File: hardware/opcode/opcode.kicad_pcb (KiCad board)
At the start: 4 copper layers, 60 parts, among them U1 74HC595, U10 74LVC1G32, U11 74LVC1G32, U12 SST39SF040, U13 SST39SF040, U14 SST39SF040, U15 SST39SF040, U16 74HC251, U17 74HC597, U18 74HC597, U19 74HC597, U2 74HC595, U20 74HC597, U21 74HC597, U22 74HC597, U23 74HC597, U24 74HC597, U25 74HC597, U26 74HC597, U27 74HC597, U28 74HC597, U29 74HC597, U3 74HC595, U30 74HC597, U4 74HC595, U5 74LVC1G00, U6 74LVC1G08, U7 74HC595, U8 74HC74, U9 74LVC1G00

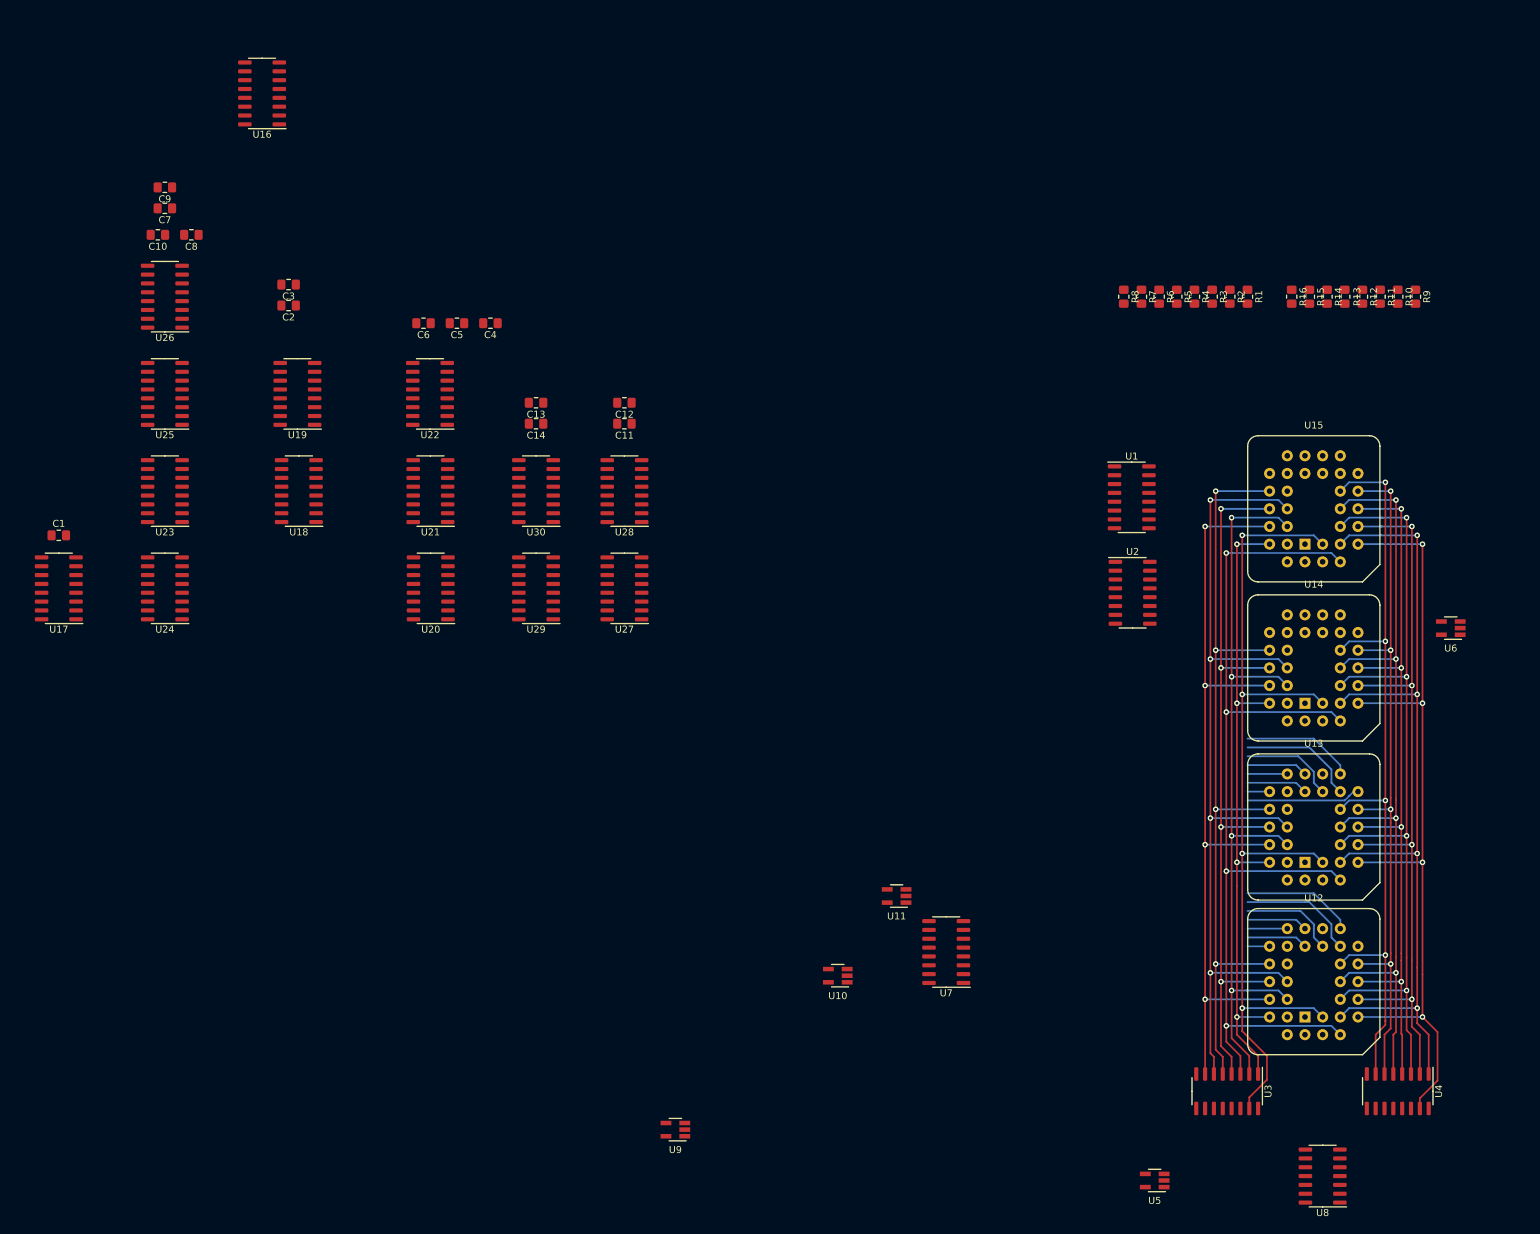
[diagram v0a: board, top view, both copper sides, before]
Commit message: Update all to Kicad 6
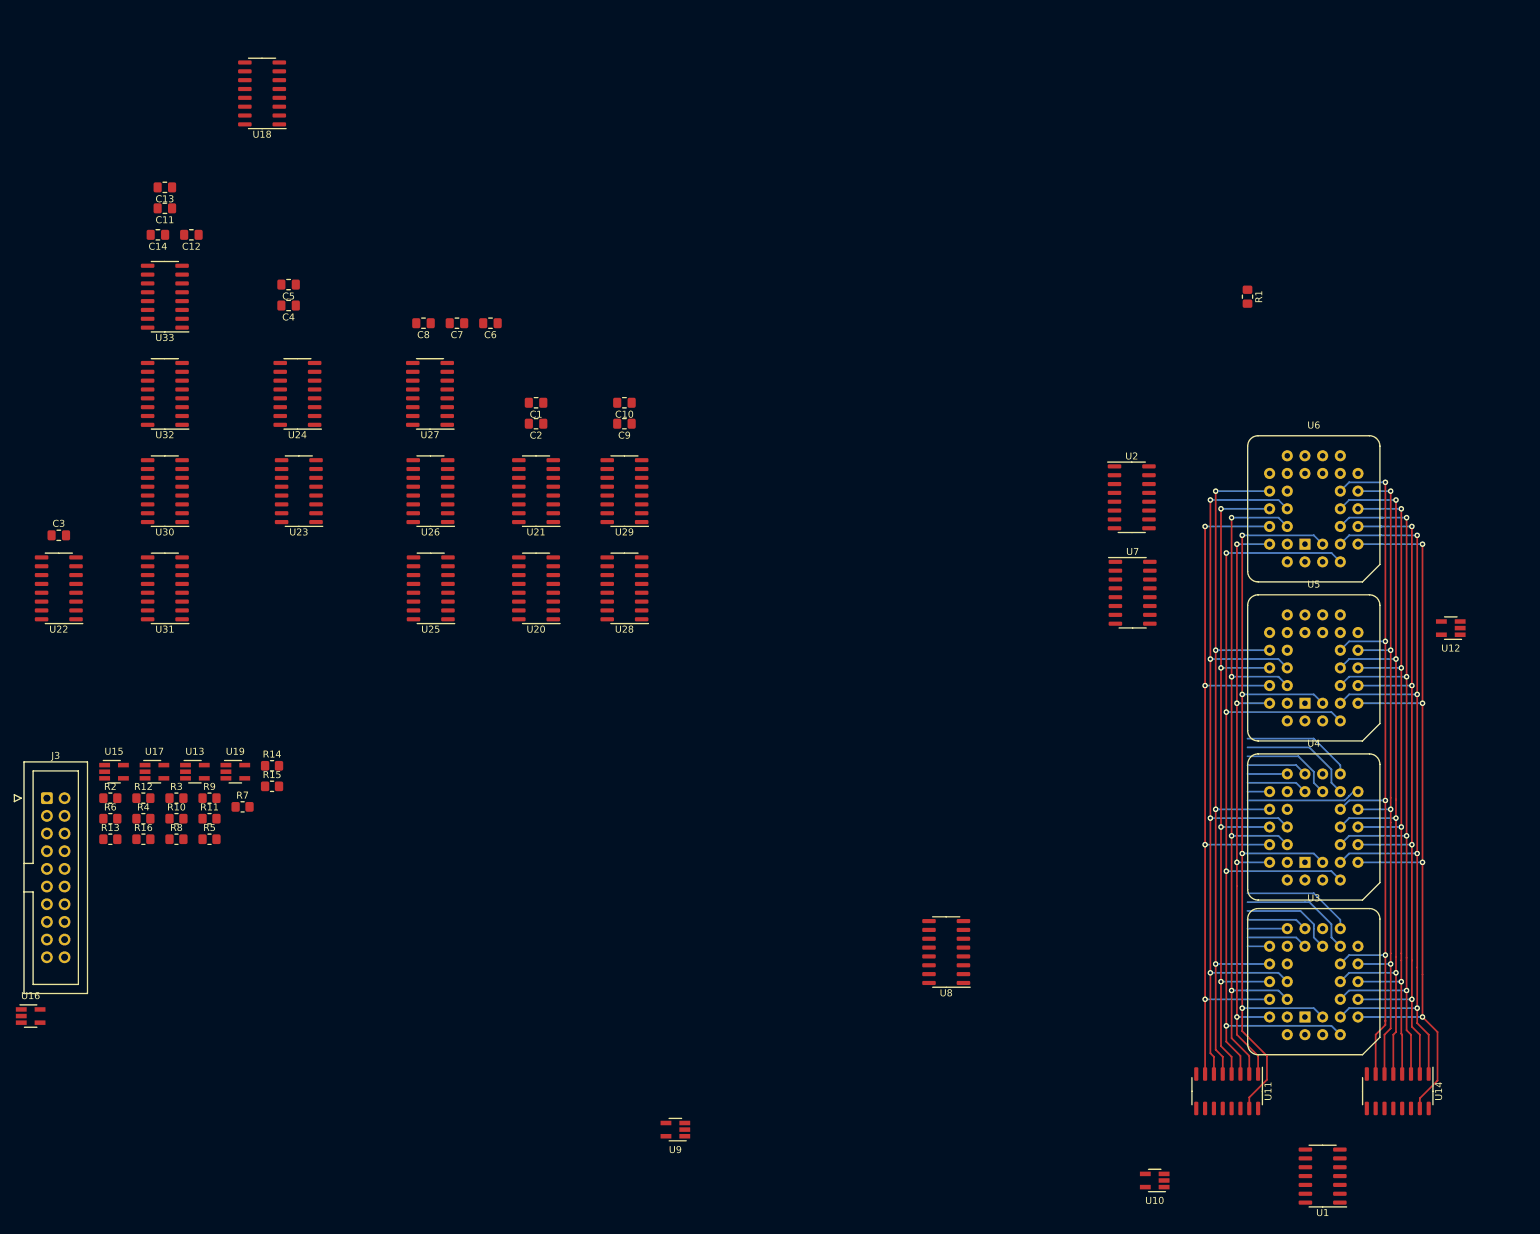
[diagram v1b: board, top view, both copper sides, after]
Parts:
- removed the U10 at (141.2, 125.5)
- removed the U11 at (149.6, 114.1)
- added J3: Conn_01x20, Connector_IDC:IDC-Header_2x10_P2.54mm_Vertical, F.Cu at (27.5, 100.0)
- added U13: 74LVC1G32, Package_TO_SOT_SMD:SOT-23-5_HandSoldering, F.Cu at (48.8, 96.2)
- added U15: 74LVC1G32, Package_TO_SOT_SMD:SOT-23-5_HandSoldering, F.Cu at (37.1, 96.2)
- added U16: 74LVC1G32, Package_TO_SOT_SMD:SOT-23-5_HandSoldering, F.Cu at (25.2, 131.3)
- added U17: 74LVC1G08, Package_TO_SOT_SMD:SOT-23-5_HandSoldering, F.Cu at (43.0, 96.2)
- added U19: 74LVC1G32, Package_TO_SOT_SMD:SOT-23-5_HandSoldering, F.Cu at (54.6, 96.2)
- moved R13 193.8 mm to (36.6, 105.9), turned to 0 degrees
- moved R10 190.9 mm to (46.1, 103.0), turned to 0 degrees
- moved R12 189.4 mm to (41.4, 100.0), turned to 0 degrees
- moved R9 187.7 mm to (50.9, 100.0), turned to 0 degrees
- moved R11 184.2 mm to (50.9, 103.0), turned to 0 degrees
- moved R16 182.5 mm to (41.4, 105.9), turned to 0 degrees
- moved R2 176.3 mm to (36.6, 100.0), turned to 0 degrees
- moved R4 168.6 mm to (41.4, 103.0), turned to 0 degrees
- moved R6 168.3 mm to (36.6, 103.0), turned to 0 degrees
- moved R14 165.9 mm to (59.9, 95.3), turned to 0 degrees
- moved R3 165.4 mm to (46.1, 100.0), turned to 0 degrees
- moved R15 164.8 mm to (59.9, 98.3), turned to 0 degrees
- moved R5 159.4 mm to (50.9, 105.9), turned to 0 degrees
- moved R8 156.9 mm to (46.1, 105.9), turned to 0 degrees
- moved R7 148.5 mm to (55.6, 101.2), turned to 0 degrees
- renumbered C13 to C1, C12 to C10, C7 to C11, C8 to C12, C9 to C13, C10 to C14, C14 to C2, C1 to C3, C2 to C4, C3 to C5, C4 to C6, C5 to C7, C6 to C8, C11 to C9, U8 to U1, U5 to U10, U3 to U11, U6 to U12, U4 to U14, U16 to U18, U1 to U2, U29 to U20, U30 to U21, U17 to U22, U18 to U23, U19 to U24, U20 to U25, U21 to U26, U22 to U27, U27 to U28, U28 to U29, U12 to U3, U23 to U30, U24 to U31, U25 to U32, U26 to U33, U13 to U4, U14 to U5, U15 to U6, U2 to U7, U7 to U8
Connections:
- U1 pad 14: Net-(U8-Pad14) -> unconnected-(U1-Pad14)
- U1 pad 6: Net-(U8-Pad6) -> unconnected-(U1-Pad6)
- U1 pad 7: Net-(U8-Pad7) -> unconnected-(U1-Pad7)
- U1 pad 9: Net-(U8-Pad9) -> unconnected-(U1-Pad9)
- U10 pad 3: Net-(U5-Pad3) -> unconnected-(U10-Pad3)
- U10 pad 5: Net-(U5-Pad5) -> unconnected-(U10-Pad5)
- U12 pad 3: Net-(U6-Pad3) -> unconnected-(U12-Pad3)
- U12 pad 5: Net-(U6-Pad5) -> unconnected-(U12-Pad5)
- U14 pad 9: Net-(U4-Pad9) -> unconnected-(U14-Pad9)
- U18 pad 6: Net-(U16-Pad6) -> unconnected-(U18-Pad6)
- U2 pad 13: /COMPR -> /COMPR_~{OE}
- U7 pad 13: /COMPR -> /COMPR_~{OE}
- U8 pad 1: Net-(U7-Pad1) -> unconnected-(U8-Pad1)
- U8 pad 15: Net-(U7-Pad15) -> unconnected-(U8-Pad15)
- U8 pad 2: Net-(U7-Pad2) -> unconnected-(U8-Pad2)
- U8 pad 3: Net-(U7-Pad3) -> unconnected-(U8-Pad3)
- U8 pad 4: Net-(U7-Pad4) -> unconnected-(U8-Pad4)
- U8 pad 5: Net-(U7-Pad5) -> unconnected-(U8-Pad5)
- U8 pad 9: Net-(U7-Pad9) -> unconnected-(U8-Pad9)
- U9 pad 3: Net-(U9-Pad3) -> unconnected-(U9-Pad3)
- U9 pad 5: Net-(U9-Pad5) -> unconnected-(U9-Pad5)

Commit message: Updated schematics and pcbs
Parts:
- added R17: 10k, riscv-serial:Jumper_3_R_0805, F.Cu at (183.5, 114.3)
- added R18: 10k, riscv-serial:Jumper_3_R_0805, F.Cu at (181.6, 91.4)
- added R19: 10k, riscv-serial:Jumper_3_R_0805, F.Cu at (181.6, 88.9)
- added R20: 10k, riscv-serial:Jumper_3_R_0805, F.Cu at (181.6, 86.4)
- added R21: 10k, riscv-serial:Jumper_3_R_0805, F.Cu at (181.6, 83.8)
- added R22: 10k, riscv-serial:Jumper_3_R_0805, F.Cu at (181.6, 81.3)
- added R23: 10k, riscv-serial:Jumper_3_R_0805, F.Cu at (181.6, 78.7)
- added R24: 10k, riscv-serial:Jumper_3_R_0805, F.Cu at (181.6, 76.2)
- added R25: 10k, riscv-serial:Jumper_3_R_0805, F.Cu at (181.6, 73.7)
- added R26: 10k, riscv-serial:Jumper_3_R_0805, F.Cu at (181.6, 71.1)
- added R27: 10k, riscv-serial:Jumper_3_R_0805, F.Cu at (181.6, 68.6)
- added R28: 10k, riscv-serial:Jumper_3_R_0805, F.Cu at (181.6, 66.0)
- added R29: 10k, riscv-serial:Jumper_3_R_0805, F.Cu at (181.6, 63.5)
- added R30: 10k, riscv-serial:Jumper_3_R_0805, F.Cu at (181.6, 61.0)
- added R31: 10k, riscv-serial:Jumper_3_R_0805, F.Cu at (181.6, 58.4)
- added R32: 10k, riscv-serial:Jumper_3_R_0805, F.Cu at (181.6, 55.9)
- R1, R10, R11, R12, R13, R14, R15, R16, R2, R3, R4, R5, R6, R7, R8, R9: footprint Resistor_SMD:R_0805_2012Metric_Pad1.20x1.40mm_HandSolder -> riscv-serial:Jumper_3_R_0805
- moved R6 197.6 mm to (232.4, 129.5), turned to 180 degrees
- moved R2 196.8 mm to (232.4, 119.4), turned to 180 degrees
- moved R4 192.3 mm to (232.4, 124.5)
- moved R8 188.5 mm to (232.4, 134.6)
- moved R3 187.6 mm to (232.4, 121.9), turned to 180 degrees
- moved R5 182.8 mm to (232.4, 127.0)
- moved R7 179.5 mm to (232.4, 132.1), turned to 180 degrees
- moved R13 148.1 mm to (183.5, 124.5), turned to 180 degrees
- moved R12 144.7 mm to (183.5, 127.0), turned to 180 degrees
- moved R16 142.6 mm to (183.5, 116.8), turned to 180 degrees
- moved R10 140.5 mm to (183.5, 132.1), turned to 180 degrees
- moved R9 137.1 mm to (183.5, 134.6), turned to 180 degrees
- moved R11 135.3 mm to (183.5, 129.5), turned to 180 degrees
- moved R14 126.5 mm to (183.5, 121.9), turned to 180 degrees
- moved R15 125.4 mm to (183.5, 119.4), turned to 180 degrees
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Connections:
- R1 pad 2: /A15 -> /A0
- R10 pad 2: /A6 -> /A9
- R11 pad 2: /A5 -> /A10
- R12 pad 2: /A4 -> /A11
- R13 pad 2: /A3 -> /A12
- R14 pad 2: /A2 -> /A13
- R15 pad 2: /A1 -> /A14
- R16 pad 1: VCC -> GND
- R16 pad 2: /A0 -> /A15
- R2 pad 1: GND -> VCC
- R2 pad 2: /A14 -> /A1
- R3 pad 2: /A13 -> /A2
- R4 pad 2: /A12 -> /A3
- R5 pad 2: /A11 -> /A4
- R6 pad 1: GND -> VCC
- R6 pad 2: /A10 -> /A5
- R7 pad 1: GND -> VCC
- R7 pad 2: /A9 -> /A6
- R8 pad 2: /A8 -> /A7
- R9 pad 2: /A7 -> /A8

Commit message: Updated opcode and step counter PCBs
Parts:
- moved R32 96.1 mm to (143.5, 144.1), turned to -90 degrees
- moved R31 92.8 mm to (146.1, 144.1), turned to -90 degrees
- moved U11 90.5 mm to (210.8, 52.7), turned to 90 degrees
- moved R30 89.5 mm to (148.6, 144.1), turned to -90 degrees
- moved U14 89.4 mm to (222.2, 52.7), turned to 90 degrees
- moved R29 86.2 mm to (151.1, 144.1), turned to -90 degrees
- moved R28 83.0 mm to (153.7, 144.1), turned to -90 degrees
- moved R27 79.7 mm to (156.2, 144.1), turned to -90 degrees
- moved R26 76.5 mm to (158.8, 144.1), turned to -90 degrees
- moved R25 73.4 mm to (161.3, 144.1), turned to -90 degrees
- moved C4 71.1 mm to (127.0, 0.00)
- moved C5 71.1 mm to (127.0, -3.01)
- moved R24 70.1 mm to (164.5, 144.1), turned to -90 degrees
- moved U6 68.3 mm to (200.7, 126.1), turned to -90 degrees
- moved R23 67.0 mm to (167.0, 144.1), turned to -90 degrees
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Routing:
- net /A0: track 113.7 -> 214.3 mm, vias 4 -> 8
- net /A1: track 102.9 -> 199.8 mm, vias 4 -> 8
- net /A3: track 106.2 -> 186.1 mm
- net /A2: track 116.8 -> 188.5 mm, vias 4 -> 8
- net /A5: track 110.4 -> 169.9 mm
- net /A10: track 115.2 -> 166.8 mm
- net /A4: track 120.8 -> 171.7 mm, vias 4 -> 8
- net /A11: track 109.8 -> 154.4 mm, vias 4 -> 8
- net /A14: track 96.2 -> 130.1 mm
- net /A13: track 115.2 -> 145.6 mm, vias 4 -> 8
- net /B10: track 17.1 -> 0.00 mm
- net /B8: track 16.4 -> 0.00 mm
- net /B9: track 16.2 -> 0.00 mm
- net /B1: track 16.2 -> 1.40 mm
- net /A12: track 143.3 -> 128.7 mm
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- added copper zone on In1.Cu, net GND
- added copper zone on In2.Cu, net VCC
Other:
- board outline added: 101.6 x 101.6 mm
